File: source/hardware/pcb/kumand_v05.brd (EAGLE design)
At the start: 39 x 98 mm, 45 parts, among them IC1 ATMEGA328P_TQFP, IC2 ESP-WROOM-02, J1 3X2-SMD-DOT, X1 NX8045-CRYSTAL

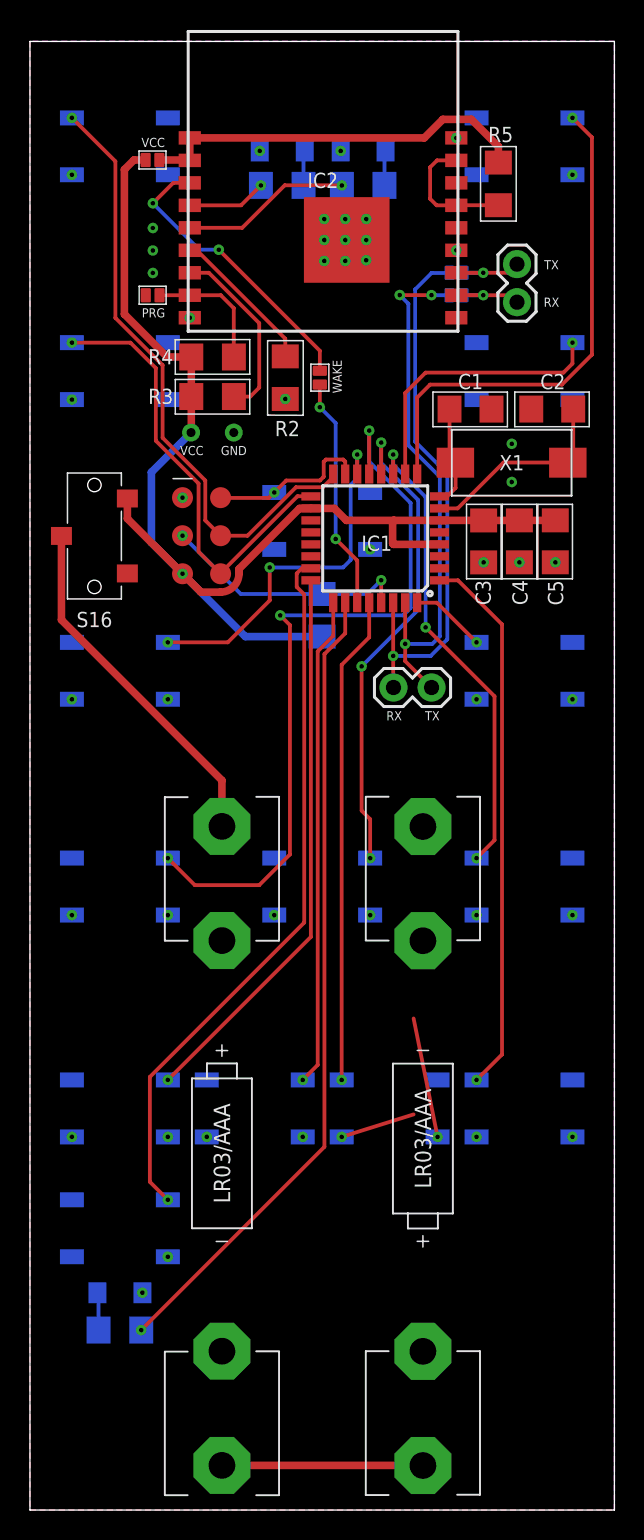
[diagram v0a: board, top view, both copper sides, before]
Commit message: Some cosmetic touch to schematic
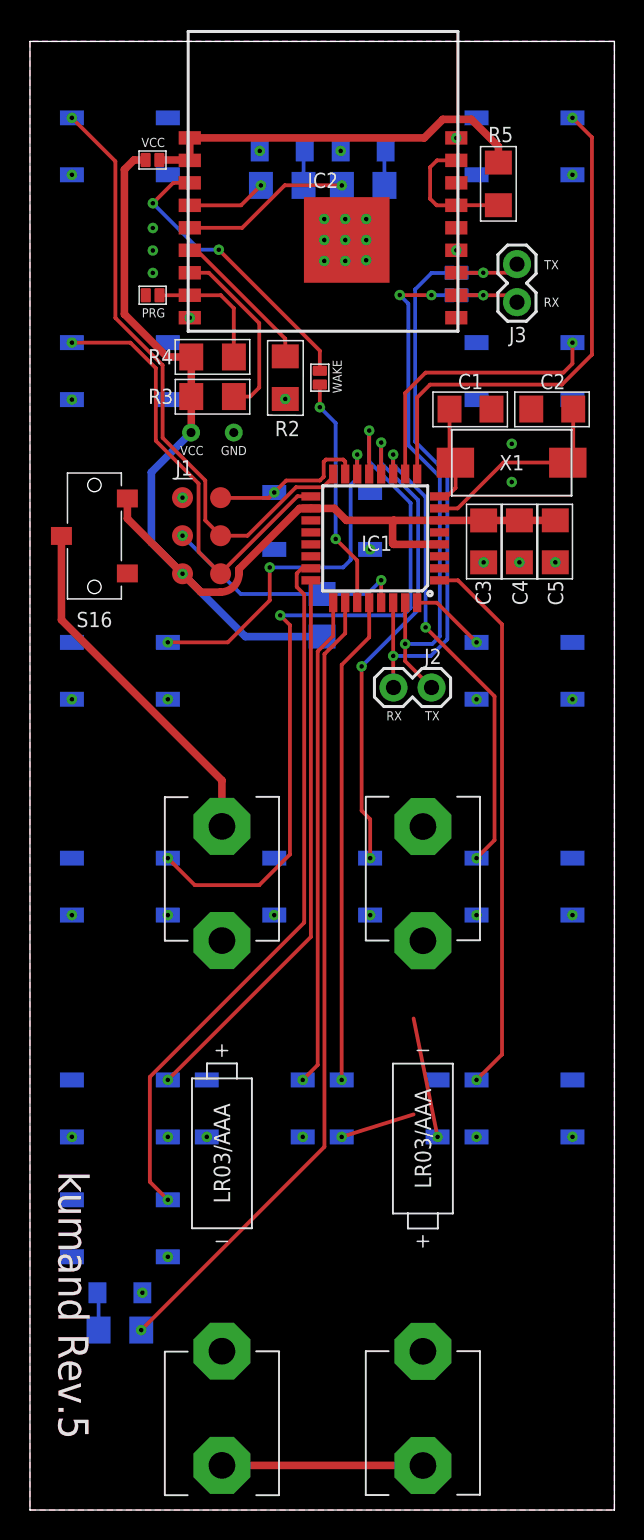
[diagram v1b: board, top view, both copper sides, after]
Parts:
- R6, R7, R8: value ? -> TBD
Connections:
- net MISO renamed S2-MISO
- net MOSI renamed S5-MOSI
- net N$11 renamed S11
- net N$12 renamed S6
- net N$13 renamed S12
- net N$16 renamed S13
- net N$17 renamed S14
- net N$18 renamed S15
- net N$23 renamed S7
- net N$5 renamed S10
- net N$6 renamed S9
- net N$7 renamed S8
- net N$8 renamed S3
- net N$9 renamed S1
- net SCK renamed S4-SCK
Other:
- board text added: "kumand Rev.5"
